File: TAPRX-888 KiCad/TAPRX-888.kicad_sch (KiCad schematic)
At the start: 120 parts, among them J1 CONN_SMA_JACK_RA, J2 CONN_SMA_JACK_RA, J3 CONN_SMA_JACK_RA, J4 CONN_SMA_JACK_RA, J5 USB-3.0, U1 AP2114H-3.3TRG1, U10 XO-19.2MHZ, U11 CYUSB3014-BZXCT, U2 AP2114H-3.3TRG1, U3 AP2114H-3.3TRG1, U4 LP5907MFX-3.3, U5 UMW AMS1117-1.2, U6 AD8370, U7 TVS-SP3011, U8 LTC2208CUP_PBF, U9 MX25L3233FM2I

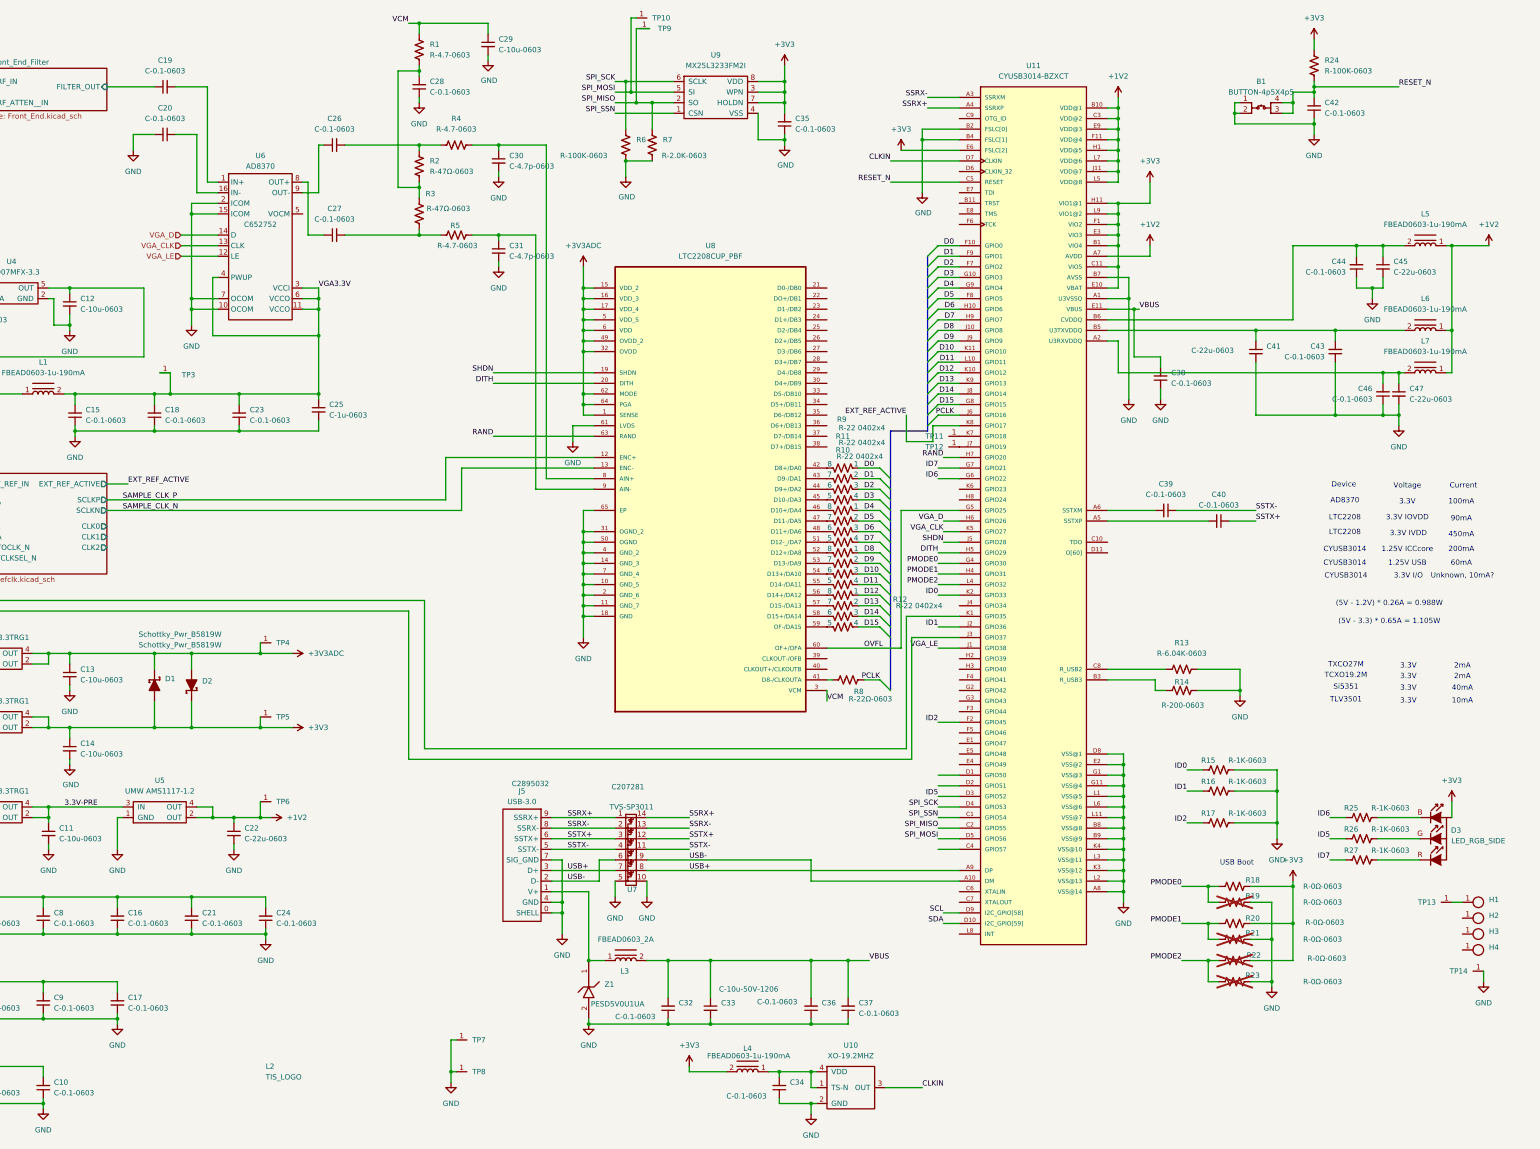
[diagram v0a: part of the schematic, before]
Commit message: acquire Pauls' latest work
in zip file 0.3a.zip.  took its files and put into TAPRX-888 KiCad, renaming them.
Moved old work to a new folder, WB6CXC previous work.
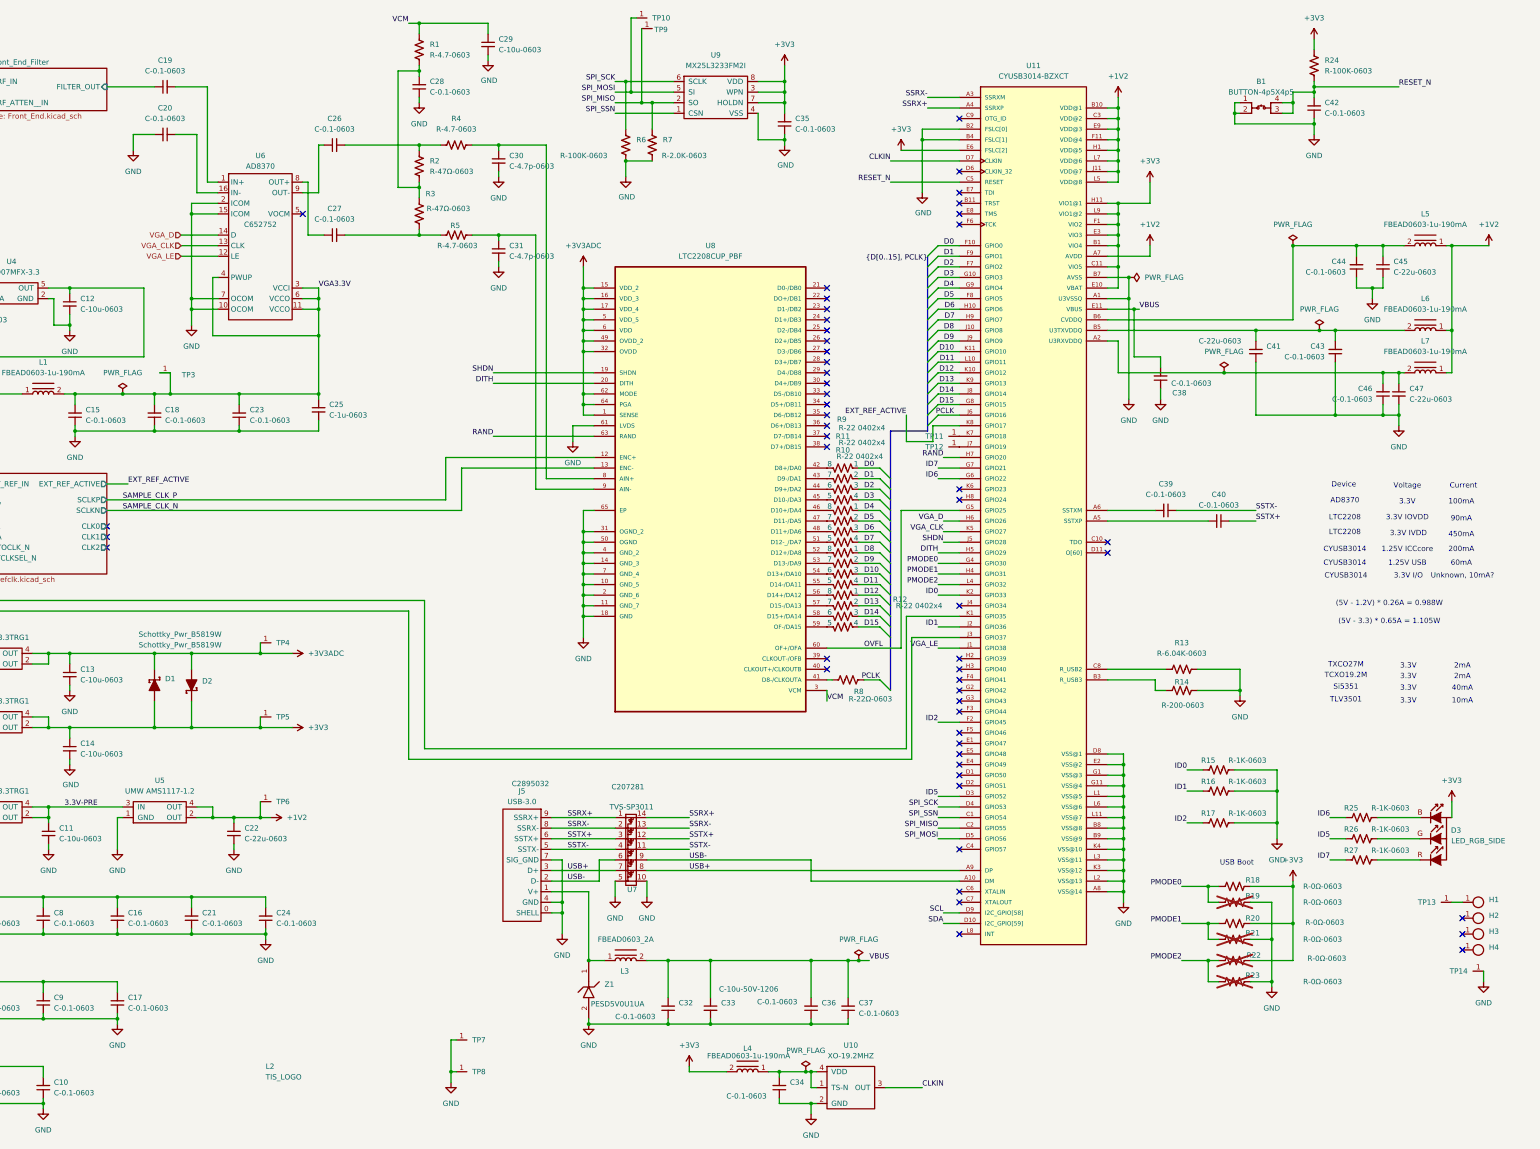
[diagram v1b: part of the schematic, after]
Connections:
- no-connect marks 0 -> 52
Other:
- moved on the sheet: TP9

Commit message: reorg to put into main directory
moved paul's v0.4 work into the main folder
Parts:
- added C77: C-0.1-0603, TIS_Footprints:C_0603, symbol capacitors:C-0.1-0603
- added J11: Conn_JTAG10-mini, TIS_Footprints:CONN-JTAG10-mini, symbol TIS:Conn_JTAG10-mini
- added R58, R59: R-47K-0603, TIS_Footprints:PAD_0603, symbol resistors:R-47K-0603
- added TP20, TP21: TP-TINY, TIS_Footprints:TP-Tiny, symbol TIS:TP-TINY
- U9: now not fitted
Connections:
- net +1V2: now also C77.2; no longer L5.1
- net +3V3: now also L5.1, J11.1 (Pin_1), R59.1
- net +3V3ADC: now also R58.1
- net GND: now also C77.1, J11.3 (Pin_3)
- net ID5: now also U11.F4 (GPIO41); no longer U11.D3 (GPIO52)
- net RESET_N: now also J11.10 (Pin_10)
- net SHDN: now also R58.2
- net TRST: now reaches U11.B11 (TRST)
- net TRST: now also J11.9 (Pin_9), R59.2
- net TDO: now reaches U11.C10 (TDO)
- net TDO: now also J11.6 (Pin_6)
- net at U11.E4 (GPIO49): now also TP21.1
- net at U11.E5 (GPIO48): now also TP20.1
- net TDI: now reaches U11.E7 (TDI)
- net TDI: now also J11.8 (Pin_8)
- net TMS: now reaches U11.E8 (TMS)
- net TMS: now also J11.2 (Pin_2)
- net TCK: now reaches U11.F6 (TCK)
- net TCK: now also J11.4 (Pin_4)
- net DIS_5351: now reaches U11.J4 (GPIO34)
- no-connect marks 52 -> 46
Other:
- sheet Clock ports: added DISABLE_5351; removed none
- moved on the sheet: C10, C35, C44, C45, L5, R6, R7, TP10, TP9

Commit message: Adding local KiCad symbol and footprint libraries to project
Adding local KiCad symbol and footprint libraries to project
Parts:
- B1: symbol TIS:BUTTON-4p5X4p5 -> Library:BUTTON-4p5X4p5
- C1, C10, C15, C16, C17, C18, C19, C2, C20, C21, C23, C24, C26, C27, C28, C3, C32, C34, C35, C36, C37, C38, C39, C40, C42, C43, C44, C46, C5, C6, C7, C77, C8, C9: symbol capacitors:C-0.1-0603 -> Library:C-0.1-0603
- C11, C12, C13, C14, C29: symbol capacitors:C-10u-0603 -> Library:C-10u-0603
- C22, C41, C45, C47: symbol capacitors:C-22u-0603 -> Library:C-22u-0603
- C25, C4: symbol capacitors:C-1u-0603 -> Library:C-1u-0603
- C30, C31: symbol capacitors:C-4.7p-0603 -> Library:C-4.7p-0603
- C33: symbol capacitors:C-10u-1206 -> Library:C-10u-1206
- D1, D2: symbol TIS:Schottky_Pwr_B5819W -> Library:Schottky_Pwr_B5819W
- D3: symbol TIS:LED_RGB_SIDE -> Library:LED_RGB_SIDE
- H1, H2, H3, H4: symbol TIS:Hole-M2.5 -> Library:Hole-M2.5
- J1, J2, J3, J4: symbol TIS:CONN_SMA_JACK_RA -> Library:CONN_SMA_JACK_RA
- J11: symbol TIS:Conn_JTAG10-mini -> Library:Conn_JTAG10-mini
- J5: symbol TIS:USB-3.0 -> Library:USB-3.0
- L1, L4, L5, L6, L7: symbol TIS:FBEAD0603-1u-190mA -> Library:FBEAD0603-1u-190mA
- L2: symbol TIS:TIS_LOGO -> Library:TIS_LOGO
- L3: symbol TIS:FBEAD0603_2A -> Library:FBEAD0603_2A
- R1, R4, R5: symbol resistors:R-4.7-0603 -> Library:R-4.7-0603
- R10, R11, R12, R9: symbol resistors:R-22 0402x4 -> Library:R-22 0402x4
- R13: symbol resistors:R-6.04K-0603 -> Library:R-6.04K-0603
- R14: symbol resistors:R-200-0603 -> Library:R-200-0603
- R15, R16, R17, R25, R26, R27: symbol resistors:R-1K-0603 -> Library:R-1K-0603
- R18, R19, R20, R21, R22, R23: symbol resistors:R-0Ω-0603 -> Library:R-0Ω-0603
- R2, R3: symbol resistors:R-47Ω-0603 -> Library:R-47Ω-0603
- R24, R6: symbol resistors:R-100K-0603 -> Library:R-100K-0603
- R58, R59: symbol resistors:R-47K-0603 -> Library:R-47K-0603
- R7: symbol resistors:R-2.0K-0603 -> Library:R-2.0K-0603
- R8: symbol resistors:R-22Ω-0603 -> Library:R-22Ω-0603
- TP1, TP10, TP11, TP12, TP13, TP14, TP2, TP3, TP4, TP5, TP6, TP7, TP8, TP9: symbol TIS:TP -> Library:TP
- TP20, TP21: symbol TIS:TP-TINY -> Library:TP-TINY
- U1, U2, U3: symbol TIS:VREG-3.3V-SOT223 -> Library:VREG-3.3V-SOT223
- U10: symbol TIS:XO-19.2MHz -> Library:XO-19.2MHz
- U11: symbol X-888:CYUSB3014-BZXCT -> Library:CYUSB3014-BZXCT
- U4: symbol TIS:LP5907MFX-3.3 -> Library:LP5907MFX-3.3
- U5: symbol TIS:VREG-1.2V-SOT223 -> Library:VREG-1.2V-SOT223
- U6: symbol TIS:AD8370 -> Library:AD8370
- U7: symbol TIS:TVS-SP3011 -> Library:TVS-SP3011
- U8: symbol X-888:LTC2208CUP_PBF -> Library:LTC2208CUP_PBF
- U9: symbol TIS:Flash_MX25L3233FM21 -> Library:Flash_MX25L3233FM21
- Z1: symbol TIS:ESD-PESD5V0U1UA -> Library:ESD-PESD5V0U1UA

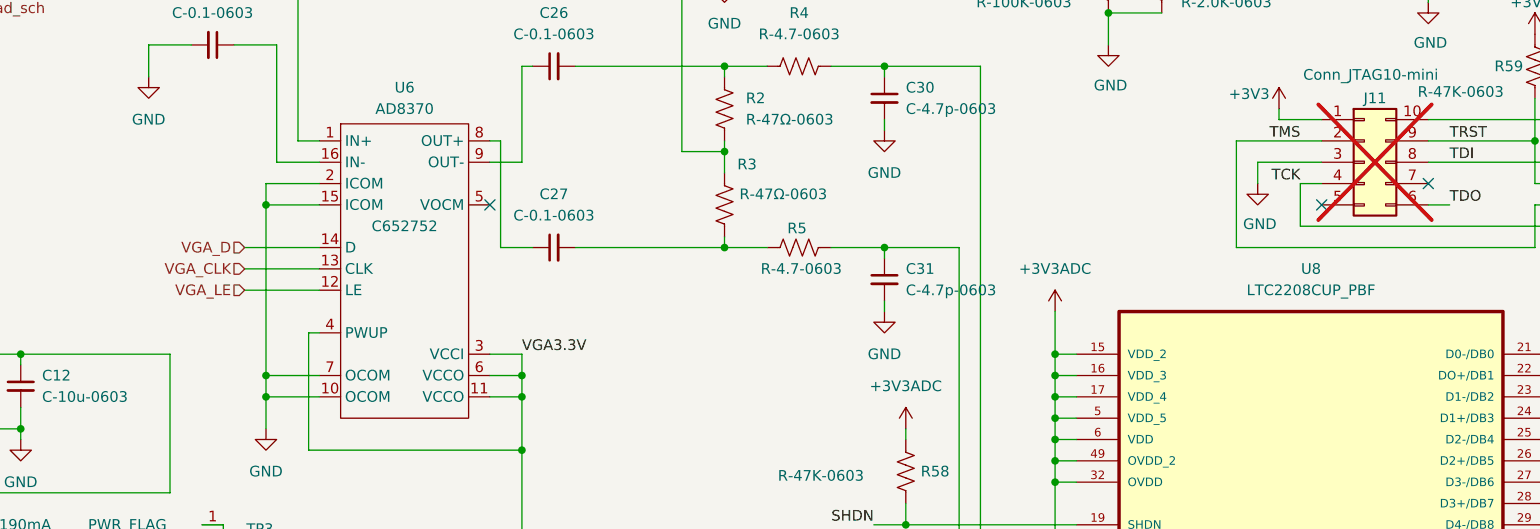
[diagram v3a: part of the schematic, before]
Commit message: Updated ADC component data, fixed KiCad v10 zone issue
ADC name and LCSC # updated
KiCad v10 DRC changes - zone overlap and priority check failed (board OK, just DRC issue).  Fixed DRC by merging zones.
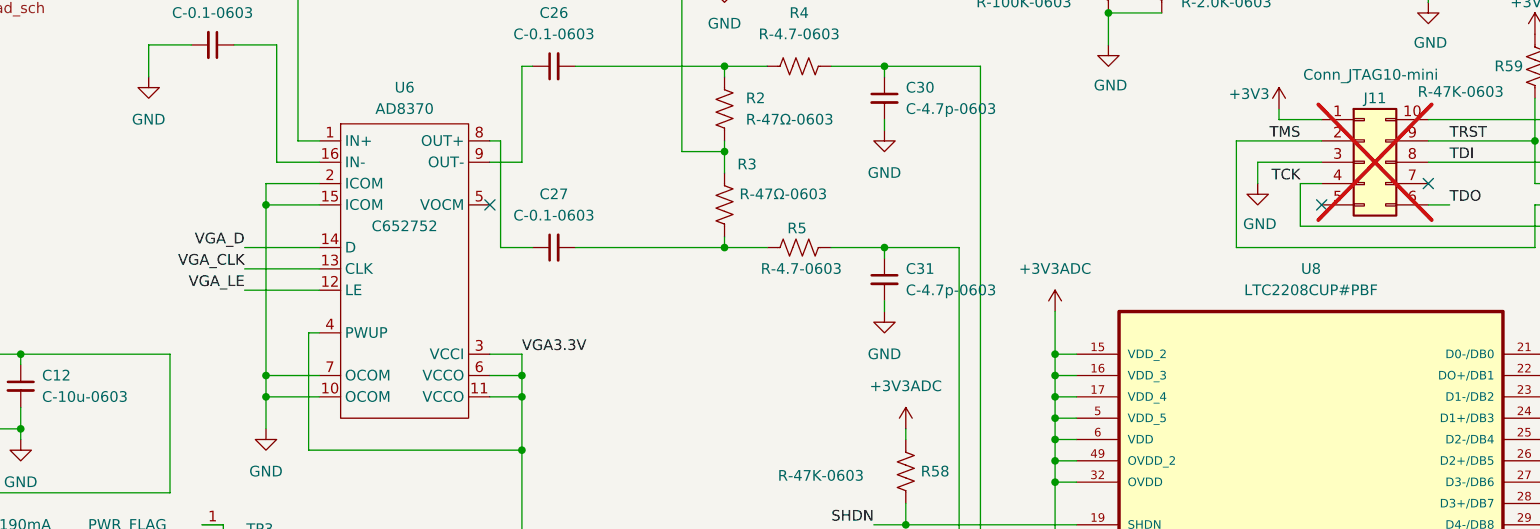
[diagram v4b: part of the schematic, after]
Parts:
- H1, H2, H3, H4: value ~ -> (none)
- U8: value LTC2208CUP_PBF -> LTC2208CUP#PBF; LCSC Part # C679544 -> C7458386
